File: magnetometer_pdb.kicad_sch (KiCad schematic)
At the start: 59 parts, among them J1 Screw_Terminal_01x02, J10 Screw_Terminal_01x02, J11 Screw_Terminal_01x02, J12 Screw_Terminal_01x02, J13 Screw_Terminal_01x02, J14 Screw_Terminal_01x02, J2 Screw_Terminal_01x02, J3 Screw_Terminal_01x02, J4 Screw_Terminal_01x02, J6 Conn_01x02_Pin, J7 Conn_01x02_Pin, J8 Conn_01x02_Pin, J9 Screw_Terminal_01x02, U2 L78L09_SO8, U3 ${SIM.PARAMS}, U4 ${SIM.PARAMS}, U5 ${SIM.PARAMS}, U6 ${SIM.PARAMS}

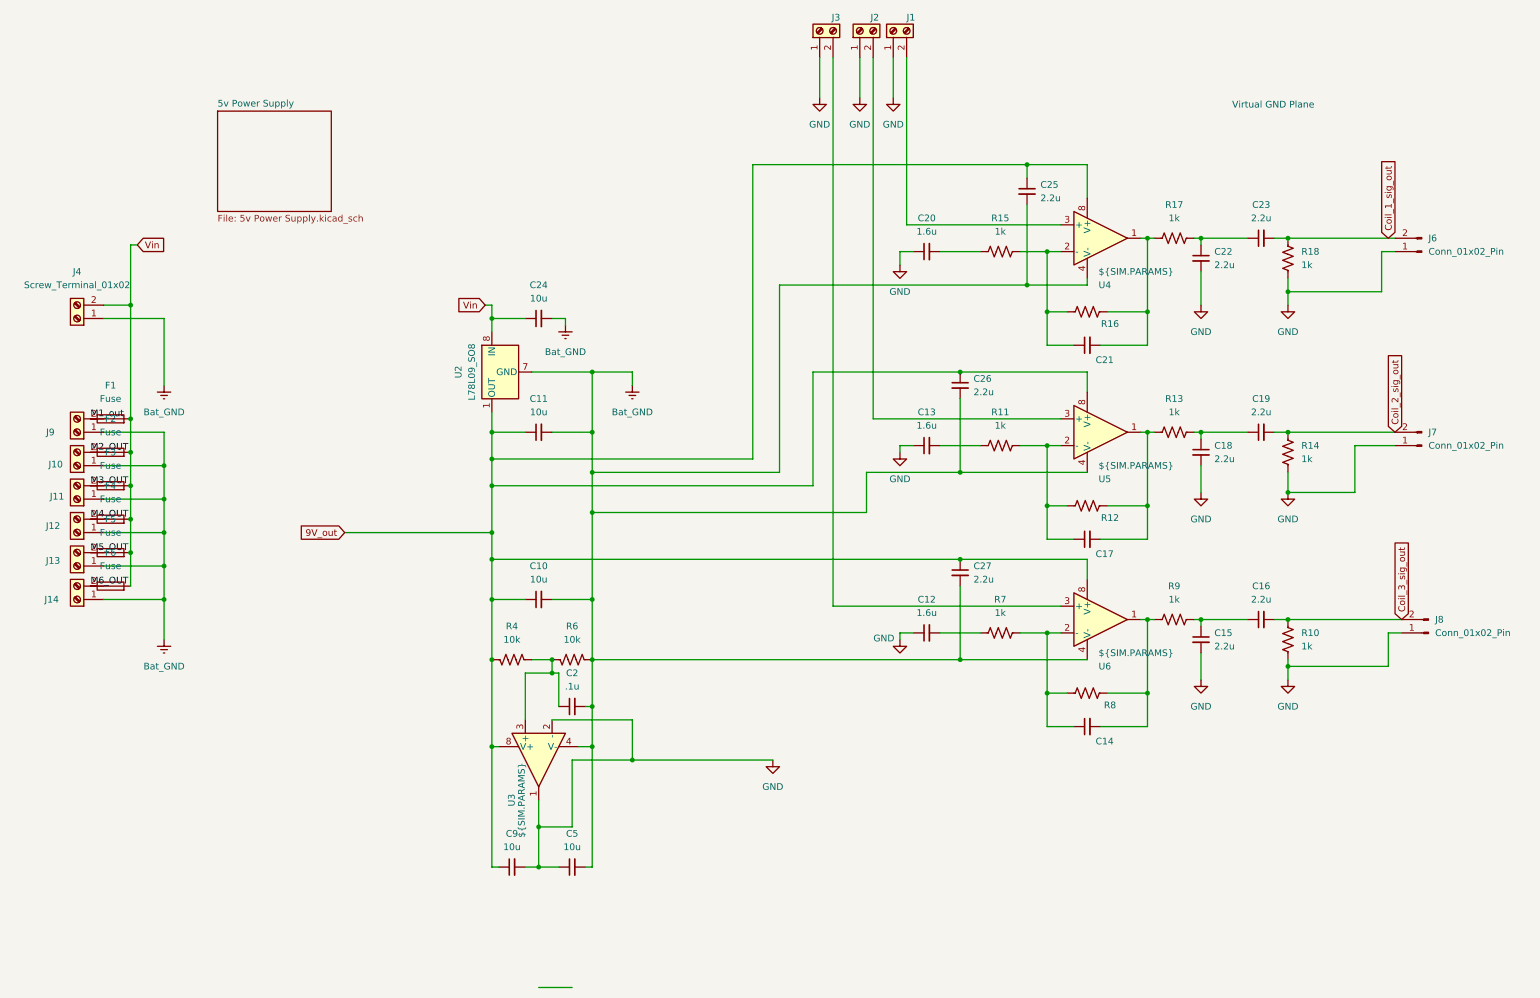
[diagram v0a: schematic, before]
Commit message: Simplified Schematic and finished PCB
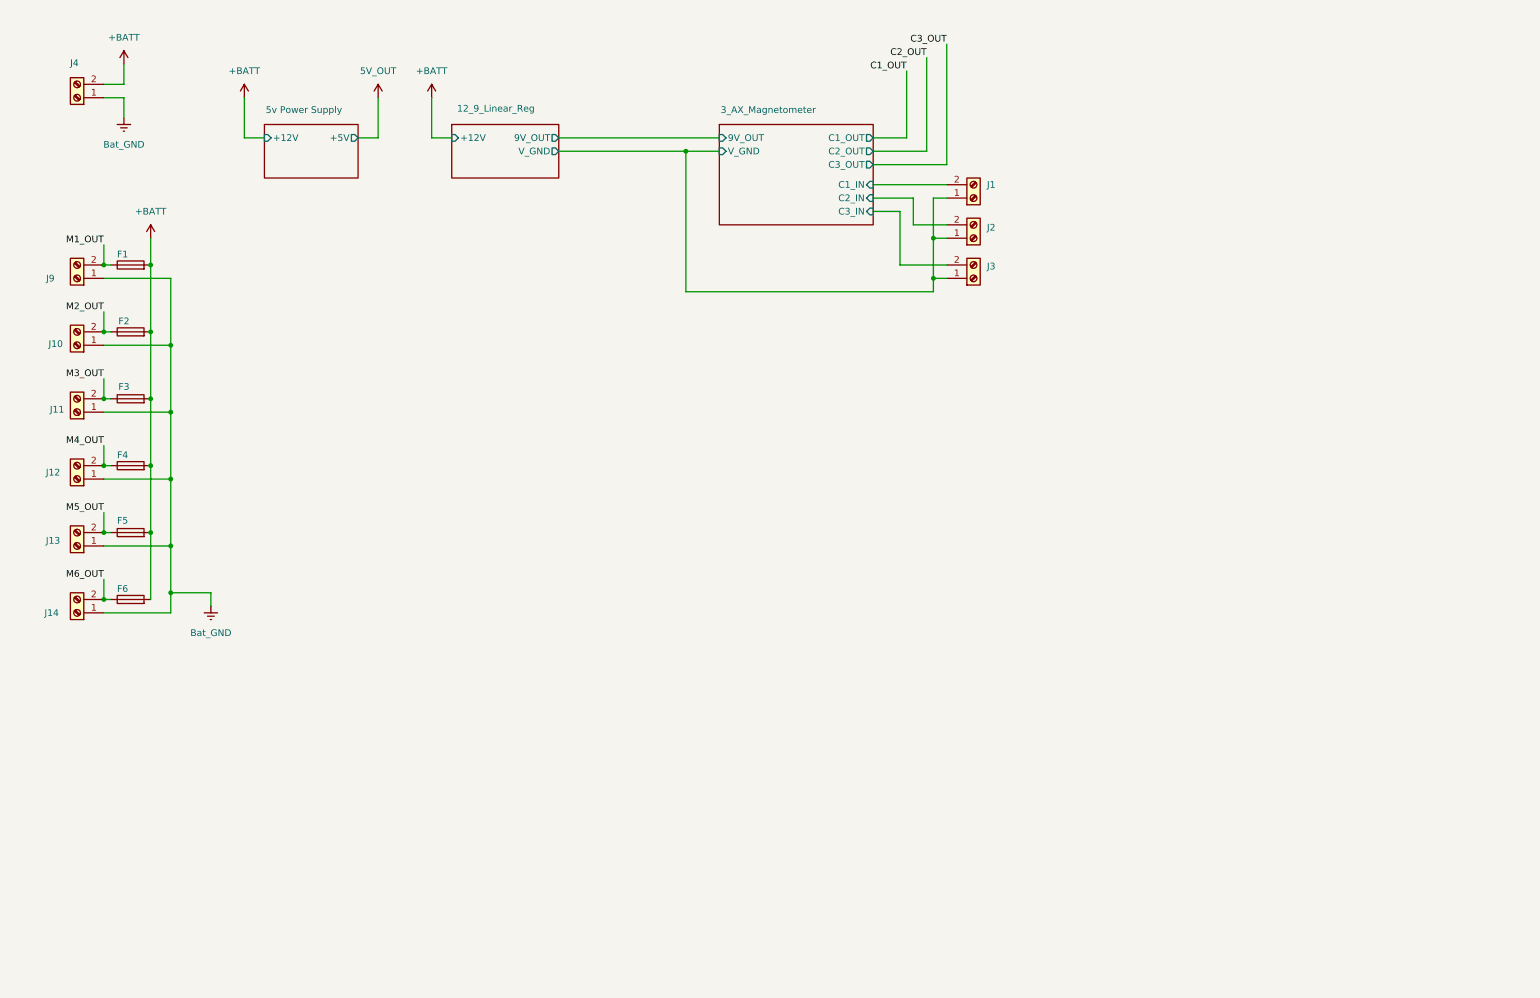
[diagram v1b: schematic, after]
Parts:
- removed C10, C11, C24, C5, C9: 10u, Capacitor_SMD:C_0805_2012Metric_Pad1.18x1.45mm_HandSolder, symbol Device:C_Small
- removed C12, C13, C20: 1.6u, Capacitor_SMD:C_0805_2012Metric_Pad1.18x1.45mm_HandSolder, symbol Device:C_Small
- removed C14, C17, C2, C21: .1u, Capacitor_SMD:C_0805_2012Metric_Pad1.18x1.45mm_HandSolder, symbol Device:C_Small
- removed C15, C16, C18, C19, C22, C23, C25, C26, C27: 2.2u, Capacitor_SMD:C_0805_2012Metric_Pad1.18x1.45mm_HandSolder, symbol Device:C_Small
- removed J6, J7, J8: Conn_01x02_Pin, Connector_Wire:SolderWire-0.5sqmm_1x02_P4.6mm_D0.9mm_OD2.1mm, symbol Connector:Conn_01x02_Pin
- removed R10, R11, R13, R14, R15, R17, R18, R7, R9: 1k, Resistor_SMD:R_0805_2012Metric_Pad1.20x1.40mm_HandSolder, symbol Device:R_US
- removed R12, R16, R8: 200k, Resistor_SMD:R_0805_2012Metric_Pad1.20x1.40mm_HandSolder, symbol Device:R_US
- removed R4, R6: 10k, Resistor_SMD:R_0805_2012Metric_Pad1.20x1.40mm_HandSolder, symbol Device:R_US
- removed U2: L78L09_SO8, Package_SO:SOIC-8_3.9x4.9mm_P1.27mm, symbol Regulator_Linear:L78L09_SO8
- removed U3, U4, U5, U6: ${SIM.PARAMS}, Package_SO:TL072ACP, symbol Simulation_SPICE:OPAMP
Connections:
- net M1_out is gone; now on net M1_OUT: F1.1
- net M2_OUT: now also J10.2 (Pin_2)
- net M3_OUT: now also J11.2 (Pin_2)
- net M4_OUT: now also J12.2 (Pin_2)
- net M5_OUT: now also J13.2 (Pin_2)
- net M6_OUT: now also J14.2 (Pin_2)
- net 3_AX_Magnetometer/C1_IN: now reaches J1.2 (Pin_2)
- net 3_AX_Magnetometer/C2_IN: now reaches J2.2 (Pin_2)
- net 3_AX_Magnetometer/C3_IN: now reaches J3.2 (Pin_2)
- net M1_OUT: now reaches J9.2 (Pin_2)
- net GND renamed 12_9_Linear_Reg/V_GND
- net Vin renamed +BATT
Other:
- added sheet 12_9_Linear_Reg (12_9_Linear_Reg.kicad_sch)
- added sheet 3_AX_Magnetometer (magnetometer.kicad_sch)
- sheet 5v Power Supply ports: added +12V, +5V; removed none
- note removed: "Virtual GND Plane"
- company: (none) -> Hexapus
- title: (none) -> Power Distribution and Magnetometer Circuit
- moved on the sheet: F1, F2, F3, F4, F5, F6, J1, J10, J11, J12, J13, J14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

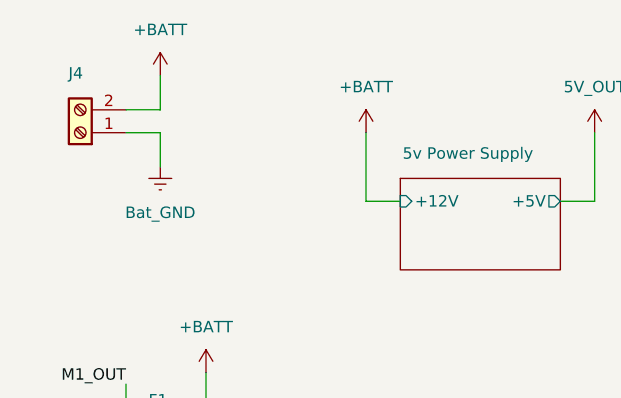
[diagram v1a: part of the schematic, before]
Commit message: Added bypass caps for 5V output and battery to protect from in rush and back emf
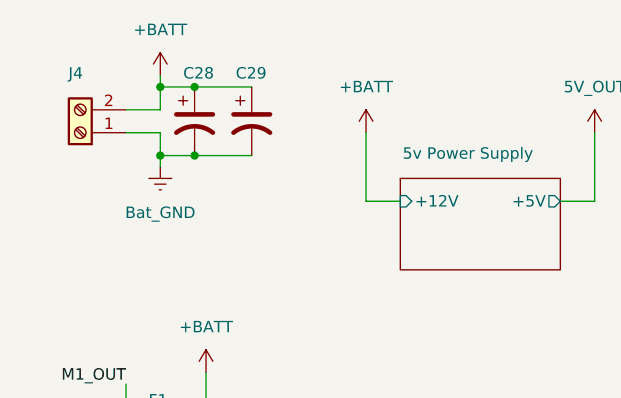
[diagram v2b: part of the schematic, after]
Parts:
- added C28: 100u, Capacitor_THT:CP_Radial_D6.3mm_P2.50mm, symbol Device:C_Polarized_US
- added C29: C_Polarized_US, Capacitor_THT:CP_Radial_D6.3mm_P2.50mm, symbol Device:C_Polarized_US
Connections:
- net +BATT: now also C28.1, C29.1
- net Bat_GND: now also C28.2, C29.2
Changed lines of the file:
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@@
+	)
+	(junction
+		(at 35.56 26.67)
+		(diameter 0)
+		(color 0 0 0 0)
+	)
+	(junction
+		(at 31.75 34.29)
+		(diameter 0)
+		(color 0 0 0 0)
 	)
 	(junction
@@
 	)
 	(junction
+		(at 35.56 34.29)
+		(diameter 0)
+		(color 0 0 0 0)
+	)
+	(junction
 		(at 40.64 78.74)
 		(diameter 0)
@@
 	)
 	(junction
+		(at 31.75 26.67)
+		(diameter 0)
+		(color 0 0 0 0)
+	)
+	(junction
 		(at 27.94 88.9)
 		(diameter 0)
@@
 	(wire
 		(pts
-			(xy 31.75 35.56) (xy 31.75 31.75)
+			(xy 31.75 35.56) (xy 31.75 34.29)
 		)
 		(stroke
@@
 	(wire
 		(pts
+			(xy 31.75 34.29) (xy 35.56 34.29)
+		)
+		(stroke
+			(width 0)
+			(type default)
+		)
+	)
+	(wire
+		(pts
 			(xy 36.83 127) (xy 36.83 114.3)
 		)
@@
 	(wire
 		(pts
+			(xy 31.75 34.29) (xy 31.75 31.75)
+		)
+		(stroke
+			(width 0)
+			(type default)
+		)
+	)
+	(wire
+		(pts
 			(xy 185.42 58.42) (xy 185.42 66.04)
 		)
@@
 	(wire
 		(pts
+			(xy 31.75 26.67) (xy 31.75 29.21)
+		)
+		(stroke
+			(width 0)
+			(type default)
+		)
+	)
+	(wire
+		(pts
 			(xy 58.42 39.37) (xy 54.61 39.37)
 		)
@@
 	(wire
 		(pts
+			(xy 35.56 26.67) (xy 41.91 26.67)
+		)
+		(stroke
+			(width 0)
+			(type default)
+		)
+	)
+	(wire
+		(pts
 			(xy 90.17 31.75) (xy 90.17 39.37)
 		)
@@
 	(wire
 		(pts
+			(xy 35.56 34.29) (xy 41.91 34.29)
+		)
+		(stroke
+			(width 0)
+			(type default)
+		)
+	)
+	(wire
+		(pts
 			(xy 173.99 44.45) (xy 187.96 44.45)
 		)
@@
 	(wire
 		(pts
+			(xy 31.75 26.67) (xy 35.56 26.67)
+		)
+		(stroke
+			(width 0)
+			(type default)
+		)
+	)
+	(wire
+		(pts
 			(xy 27.94 104.14) (xy 40.64 104.14)
 		)
@@
 	(wire
 		(pts
-			(xy 31.75 25.4) (xy 31.75 29.21)
+			(xy 31.75 25.4) (xy 31.75 26.67)
 		)
 		(stroke
@@
 	)
 	(symbol
+		(lib_id "Device:C_Polarized_US")
+		(at 35.56 30.48 0)
+		(unit 1)
+		(exclude_from_sim no)
+		(in_bom yes)
+		(on_board yes)
+		(dnp no)
+		(property "Reference" "C28"
+			(at 34.29 25.146 0)
+			(effects
+				(font
+					(size 1.27 1.27)
+				)
+				(justify left)
+			)
+		)
+		(property "Value" "100u"
+			(at 39.37 31.1149 0)
+			(effects
+				(font
+					(size 1.27 1.27)
+				)
+				(justify left)
+				(hide yes)
+			)
+		)
+		(property "Footprint" "Capacitor_THT:CP_Radial_D6.3mm_P2.50mm"
+			(at 35.56 30.48 0)
+			(effects
+				(font
+					(size 1.27 1.27)
+				)
+				(hide yes)
+			)
+		)
+		(property "Datasheet" "~"
+			(at 35.56 30.48 0)
+			(effects
+				(font
+					(size 1.27 1.27)
+				)
+				(hide yes)
+			)
+		)
+		(property "Description" "Polarized capacitor, US symbol"
+			(at 35.56 30.48 0)
+			(effects
+				(font
+					(size 1.27 1.27)
+				)
+				(hide yes)
+			)
+		)
+		(pin "1"
+		)
+		(pin "2"
+		)
+		(instances
+			(project ""
+				(path "/bc0e619f-307e-4ebe-8a52-967fc0be98ce"
+					(reference "C28")
+					(unit 1)
+				)
+			)
+		)
+	)
+	(symbol
 		(lib_id "power:+BATT")
 		(at 54.61 31.75 0)
@@
 					(unit 1)
 				)
+			)
+		)
+	)
+	(symbol
+		(lib_id "Device:C_Polarized_US")
+		(at 41.91 30.48 0)
+		(unit 1)
+		(exclude_from_sim no)
+		(in_bom yes)
+		(on_board yes)
+		(dnp no)
+		(property "Reference" "C29"
+			(at 40.132 25.146 0)
+			(effects
+				(font
+					(size 1.27 1.27)
+				)
+				(justify left)
+			)
+		)
+		(property "Value" "C_Polarized_US"
+			(at 45.72 31.1149 0)
+			(effects
+				(font
+					(size 1.27 1.27)
+				)
+				(justify left)
+				(hide yes)
+			)
+		)
+		(property "Footprint" "Capacitor_THT:CP_Radial_D6.3mm_P2.50mm"
+			(at 41.91 30.48 0)
+			(effects
+				(font
+					(size 1.27 1.27)
+				)
+				(hide yes)
+			)
+		)
+		(property "Datasheet" "100u"
+			(at 41.91 30.48 0)
+			(effects
+				(font
+					(size 1.27 1.27)
+				)
+				(hide yes)
+			)
+		)
+		(property "Description" "Polarized capacitor, US symbol"
+			(at 41.91 30.48 0)
+			(effects
+				(font
+					(size 1.27 1.27)
+				)
+				(hide yes)
+			)
+		)
+		(pin "1"
+		)
+		(pin "2"
+		)
+		(instances
+			(project ""
+				(path "/bc0e619f-307e-4ebe-8a52-967fc0be98ce"
+					(reference "C29")
+					(unit 1)
+				)
